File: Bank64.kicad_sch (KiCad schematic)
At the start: 2 parts, among them U1 XCKU5P-FFVB676

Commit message: finishing schematic
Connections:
- net IO_L23N_T3U_N9_64_N: now reaches U1.AA17 (IO_L23N_T3U_N9_64_N)
- net IO_L24N_T3U_N11_64_N: now reaches U1.AA18 (IO_L24N_T3U_N11_64_N)
- net IO_L20P_T3L_N2_AD1P_64_P: now reaches U1.AA19 (IO_L20P_T3L_N2_AD1P_64_P)
- net IO_L21P_T3L_N4_AD8P_64_P: now reaches U1.AA20 (IO_L21P_T3L_N4_AD8P_64_P)
- net IO_L22P_T3U_N6_DBC_AD0P_64_P: now reaches U1.AB17 (IO_L22P_T3U_N6_DBC_AD0P_64_P)
- net IO_L20N_T3L_N3_AD1N_64_N: now reaches U1.AB19 (IO_L20N_T3L_N3_AD1N_64_N)
- net IO_L21N_T3L_N5_AD8N_64_N: now reaches U1.AB20 (IO_L21N_T3L_N5_AD8N_64_N)
- net IO_T3U_N12_64: now reaches U1.AC16 (IO_T3U_N12_64)
- net IO_L22N_T3U_N7_DBC_AD0N_64_N: now reaches U1.AC17 (IO_L22N_T3U_N7_DBC_AD0N_64_N)
- net GTY_1_P: now reaches U1.AC18 (IO_L16P_T2U_N6_QBC_AD3P_64_P)
- net GTY_3_P: now reaches U1.AD16 (IO_L18P_T2U_N10_AD2P_64_P)
- net GTY_1_N: now reaches U1.AD18 (IO_L16N_T2U_N7_QBC_AD3N_64_N)
- net GTY_3_N: now reaches U1.AE16 (IO_L18N_T2U_N11_AD2N_64_N)
- net GTY_2_P: now reaches U1.AE17 (IO_L17P_T2U_N8_AD10P_64_P)
- net GTY_2_N: now reaches U1.AF17 (IO_L17N_T2U_N9_AD10N_64_N)
- net GTY_0_P: now reaches U1.AF18 (IO_L15P_T2L_N4_AD11P_64_P)
- net GTY_0_N: now reaches U1.AF19 (IO_L15N_T2L_N5_AD11N_64_N)
- net IO_L23P_T3U_N8_64_P: now reaches U1.Y17 (IO_L23P_T3U_N8_64_P)
- net IO_L24P_T3U_N10_64_P: now reaches U1.Y18 (IO_L24P_T3U_N10_64_P)
- net IO_L19P_T3L_N0_DBC_AD9P_64_P: now reaches U1.Y20 (IO_L19P_T3L_N0_DBC_AD9P_64_P)
- net IO_L19N_T3L_N1_DBC_AD9N_64_N: now reaches U1.Y21 (IO_L19N_T3L_N1_DBC_AD9N_64_N)
- no-connect marks 0 -> 1

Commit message: sync works
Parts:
- added C258: 100n, Capacitor_SMD:C_0201_0603Metric, symbol Device:C
- added C259: 10u, Capacitor_SMD:C_0603_1608Metric, symbol Device:C
- added Y1: OB2EL89CEIC112YLC-200M, Oscillator:Oscillator_SMD_SiTime_PQFD-6L_3.2x2.5mm, symbol Oscillator:SiT9365xx-xBx-xxE
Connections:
- net D4_SYS_CLK_N: now also Y1.5 (OUT-)
- net D4_SYS_CLK_P: now also Y1.4 (OUT+)
- net GND: now also C258.2, C259.2, Y1.3 (GND)
- new net +3V3: C258.1, C259.1, Y1.1 (OE), Y1.6 (VDD)

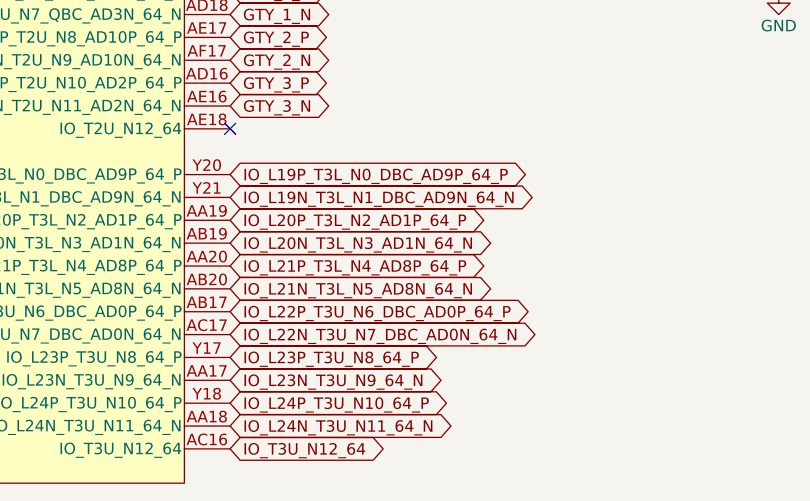
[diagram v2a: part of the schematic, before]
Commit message: change net name to of IO diff pairs, add a scripts for name modification
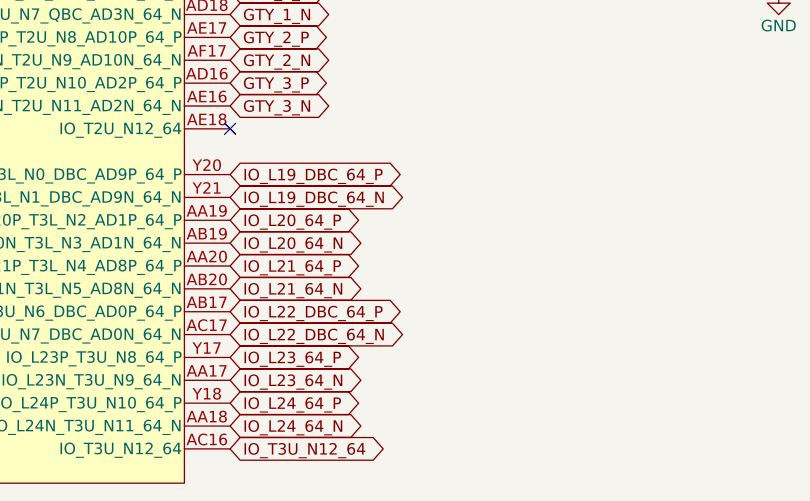
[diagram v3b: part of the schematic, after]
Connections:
- net IO_L19N_T3L_N1_DBC_AD9N_64_N renamed IO_L19_DBC_64_N
- net IO_L19P_T3L_N0_DBC_AD9P_64_P renamed IO_L19_DBC_64_P
- net IO_L20N_T3L_N3_AD1N_64_N renamed IO_L20_64_N
- net IO_L20P_T3L_N2_AD1P_64_P renamed IO_L20_64_P
- net IO_L21N_T3L_N5_AD8N_64_N renamed IO_L21_64_N
- net IO_L21P_T3L_N4_AD8P_64_P renamed IO_L21_64_P
- net IO_L22N_T3U_N7_DBC_AD0N_64_N renamed IO_L22_DBC_64_N
- net IO_L22P_T3U_N6_DBC_AD0P_64_P renamed IO_L22_DBC_64_P
- net IO_L23N_T3U_N9_64_N renamed IO_L23_64_N
- net IO_L23P_T3U_N8_64_P renamed IO_L23_64_P
- net IO_L24N_T3U_N11_64_N renamed IO_L24_64_N
- net IO_L24P_T3U_N10_64_P renamed IO_L24_64_P
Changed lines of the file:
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@@
 		)
 	)
-	(global_label "IO_L21P_T3L_N4_AD8P_64_P"
+	(global_label "IO_L21_64_P"
 		(shape bidirectional)
 		(at 85.09 148.59 0)
@@
 		)
 	)
-	(global_label "IO_L24N_T3U_N11_64_N"
+	(global_label "IO_L24_64_N"
 		(shape bidirectional)
 		(at 85.09 166.37 0)
@@
 		)
 	)
-	(global_label "IO_L22P_T3U_N6_DBC_AD0P_64_P"
+	(global_label "IO_L22_DBC_64_P"
 		(shape bidirectional)
 		(at 85.09 153.67 0)
@@
 		)
 	)
-	(global_label "IO_L20P_T3L_N2_AD1P_64_P"
+	(global_label "IO_L20_64_P"
 		(shape bidirectional)
 		(at 85.09 143.51 0)
@@
 		)
 	)
-	(global_label "IO_L23N_T3U_N9_64_N"
+	(global_label "IO_L23_64_N"
 		(shape bidirectional)
 		(at 85.09 161.29 0)
@@
 		)
 	)
-	(global_label "IO_L19P_T3L_N0_DBC_AD9P_64_P"
+	(global_label "IO_L19_DBC_64_P"
 		(shape bidirectional)
 		(at 85.09 138.43 0)
@@
 		)
 	)
-	(global_label "IO_L21N_T3L_N5_AD8N_64_N"
+	(global_label "IO_L21_64_N"
 		(shape bidirectional)
 		(at 85.09 151.13 0)
@@
 		)
 	)
-	(global_label "IO_L24P_T3U_N10_64_P"
+	(global_label "IO_L24_64_P"
 		(shape bidirectional)
 		(at 85.09 163.83 0)
@@
 		)
 	)
-	(global_label "IO_L23P_T3U_N8_64_P"
+	(global_label "IO_L23_64_P"
 		(shape bidirectional)
 		(at 85.09 158.75 0)
@@
 		)
 	)
-	(global_label "IO_L19N_T3L_N1_DBC_AD9N_64_N"
+	(global_label "IO_L19_DBC_64_N"
 		(shape bidirectional)
 		(at 85.09 140.97 0)
@@
 		)
 	)
-	(global_label "IO_L22N_T3U_N7_DBC_AD0N_64_N"
+	(global_label "IO_L22_DBC_64_N"
 		(shape bidirectional)
 		(at 85.09 156.21 0)
@@
 		)
 	)
-	(global_label "IO_L20N_T3L_N3_AD1N_64_N"
+	(global_label "IO_L20_64_N"
 		(shape bidirectional)
 		(at 85.09 146.05 0)
